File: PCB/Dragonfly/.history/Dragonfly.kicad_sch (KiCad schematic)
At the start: 201 parts, among them J1 Conn_01x04_Pin, J2 Micro_SD_Card, J3 Conn_01x02_Pin, J4 Conn_01x02_Pin, J5 Conn_01x02_Pin, J6 Conn_01x02_Pin, Q1 Q_NMOS_GDS, Q10 Q_NMOS_GDS, Q11 Q_NMOS_GDS, Q12 Q_NMOS_GDS, Q13 Q_NMOS_GDS, Q14 Q_NMOS_GDS, Q15 Q_NMOS_GDS, Q16 Q_NMOS_GDS, Q17 Q_NMOS_GDS, Q18 Q_NMOS_GDS, Q19 Q_NMOS_GDS, Q2 Q_NMOS_GDS, Q20 Q_NMOS_GDS, Q21 Q_NMOS_GDS, Q22 Q_NMOS_GDS, Q23 Q_NMOS_GDS, Q24 Q_NMOS_GDS, Q3 Q_NMOS_GDS, Q4 Q_NMOS_GDS, Q5 Q_NMOS_GDS, Q6 Q_NMOS_GDS, Q7 Q_NMOS_GDS, Q8 Q_NMOS_GDS, Q9 Q_NMOS_GDS, SW1 SW_SPST, SW2 SW_SPST, U1 STM32F405RGTx, U10 FD6288Q, U2 ICM-20602, U3 AT32F421G8U7, U4 FD6288Q, U5 AT32F421G8U7, U6 FD6288Q, U7 AT32F421G8U7, U8 FD6288Q, U9 AT32F421G8U7, X1 TSX-3225

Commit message: updates
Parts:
- removed D1: blue, symbol Device:D
- removed D2: red, symbol Device:D
- added C57, C60, C62: 10uf, symbol Device:C
- added C58: 0.01uf, symbol Device:C
- added C59: 220uf, symbol Device:C_US
- added C61, C63: 1uf, symbol Device:C
- added C64, C65: 100nf, symbol Device:C
- added D1: LED BLUE, symbol Device:LED
- added D15: 40V, 3A Schottky, Diode_SMD:D_SMC, symbol Diode:B340
- added D16: 40V, 3A Schottky, symbol Device:D_Schottky
- added D2: LED RED, symbol Device:LED
- added J7: Conn_01x02, symbol Connector_Generic:Conn_01x02
- added L2: 15uh, symbol Device:L_Ferrite
- added R87: 30.9k, symbol Device:R
- added R88: 10k, symbol Device:R
- added R89: 100k, symbol Device:R
- added U11: TPS5430DDA, Package_SO:TI_SO-PowerPAD-8_ThermalVias, symbol Regulator_Switching:TPS5430DDA
- added U12: AMS1117-3.3, Package_TO_SOT_SMD:SOT-223-3_TabPin2, symbol Regulator_Linear:AMS1117-3.3
- added U13: L78L08_SO8, Package_SO:SOIC-8_3.9x4.9mm_P1.27mm, symbol Regulator_Linear:L78L08_SO8
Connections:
- net +8V: now also C65.1, U13.1 (OUT)
- net GND: now also C57.2, C59.2, C64.2, C65.2, D1.2 (A), D15.2 (A), D2.2 (A), J7.2 (Pin_2), R88.2, U11.6 (GND), U11.9 (GNDPAD), U13.2 (GND), U13.3 (GND), U13.6 (GND), U13.7 (GND)
- net VDD33: now also C60.1, C61.1, U12.2 (VO)
- net VIN: now also C57.1, C64.1, D16.2 (A), R89.1, U11.7 (VIN), U13.8 (IN)
- net at R4.2: now also D1.1 (K)
- net at R5.2: now also D2.1 (K)
- new net: C60.2, C61.2, C62.2, C63.2
- new net: R89.2, U11.5 (EN)
- new net: R87.2, R88.1, U11.4 (VSENSE)
- new net: C58.1, U11.1 (BOOT)
- new net: C58.2, D15.1 (K), L2.1, U11.8 (PH)
- new net: D16.1 (K), J7.1 (Pin_1)
- new net VOUT: C59.1, C62.1, C63.1, L2.2, R87.1, U12.3 (VI)
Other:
- note added: "Battery connection"
- note added: "Power - Buck (5V) + LDO (3.3V)"
- moved on the sheet: C5, R1, R2, R3, R4, R5, SW1, SW2

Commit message: Update Dragonfly.kicad_sch
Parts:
- added C66, C67, C68, C69: 100nf, symbol Device:C
- added C70, C71: 47uf, symbol Device:C_Polarized
- added J10: USB_C_Receptacle_USB2.0_16P, symbol Connector:USB_C_Receptacle_USB2.0_16P
- added J8: VIN, symbol Connector:Conn_01x02_Socket
- added J9: VOUT, symbol Connector:Conn_01x02_Socket
- added R90, R91: 75 Ω, symbol Device:R
- added R92, R93: 22k, symbol Device:R
- added U14: AT7456E, SOP65P637X110-28N, symbol MAX7456EUI:MAX7456EUI+
- added Y1: 27MHZ, symbol Device:Crystal
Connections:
- net GND: now also C66.2, C67.2, C68.2, J10.A1 (GND), J10.A12 (GND), J10.B1 (GND), J10.B12 (GND), J10.SH (SHIELD), J8.2 (Pin_2), J9.2 (Pin_2), R90.2, U14.20 (AGND), U14.23 (PGND), U14.4 (DGND)
- net VIN: now also C69.1, U14.22 (VIN)
- net VOUT: now also C70.1, U14.26 (VOUT)
- net CS 1 renamed CS IMU
- net MISO renamed MISO IMU
- net MOSI renamed MOSI IMU
- net PB12 renamed CS SOD
- net CS SOD: now also U14.8 (~{CS})
- net PB13 renamed SCK SOD
- net SCK SOD: now also U14.10 (SCLK)
- net PB14 renamed MISO SOD
- net MISO SOD: now also U14.9 (SDIN)
- net PB15 renamed MOSI OSD
- net MOSI OSD: now also U14.11 (SDOUT)
- net SCK renamed SCK IMU
- new net: J9.1 (Pin_1), R91.1
- new net: C70.2, C71.2, R91.2
- new net: J10.A5 (CC1), R92.1
- new net: C69.2, J8.1 (Pin_1), R90.1
- new net: J10.B5 (CC2), R93.1
- new net +5V: J10.A4 (VBUS), J10.A9 (VBUS), J10.B4 (VBUS), J10.B9 (VBUS), R92.2, R93.2
- new net 5V: C66.1, C67.1, C68.1, U14.19 (~{RESET}), U14.21 (AVDD), U14.24 (PVDD), U14.3 (DVDD)
- new net D+: J10.A6 (D+), J10.B6 (D+)
- new net D-: J10.A7 (D-), J10.B7 (D-)
- new net SAG: C71.1, U14.25 (SAG)
- new net XTAL1: U14.5 (CLKIN), Y1.1
- new net XTAL2: U14.6 (XFB), Y1.2
- no-connect marks 44 -> 49
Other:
- note added: "OSD - AT7456E"
- note added: "USB-C 16pin"
- moved on the sheet: C20

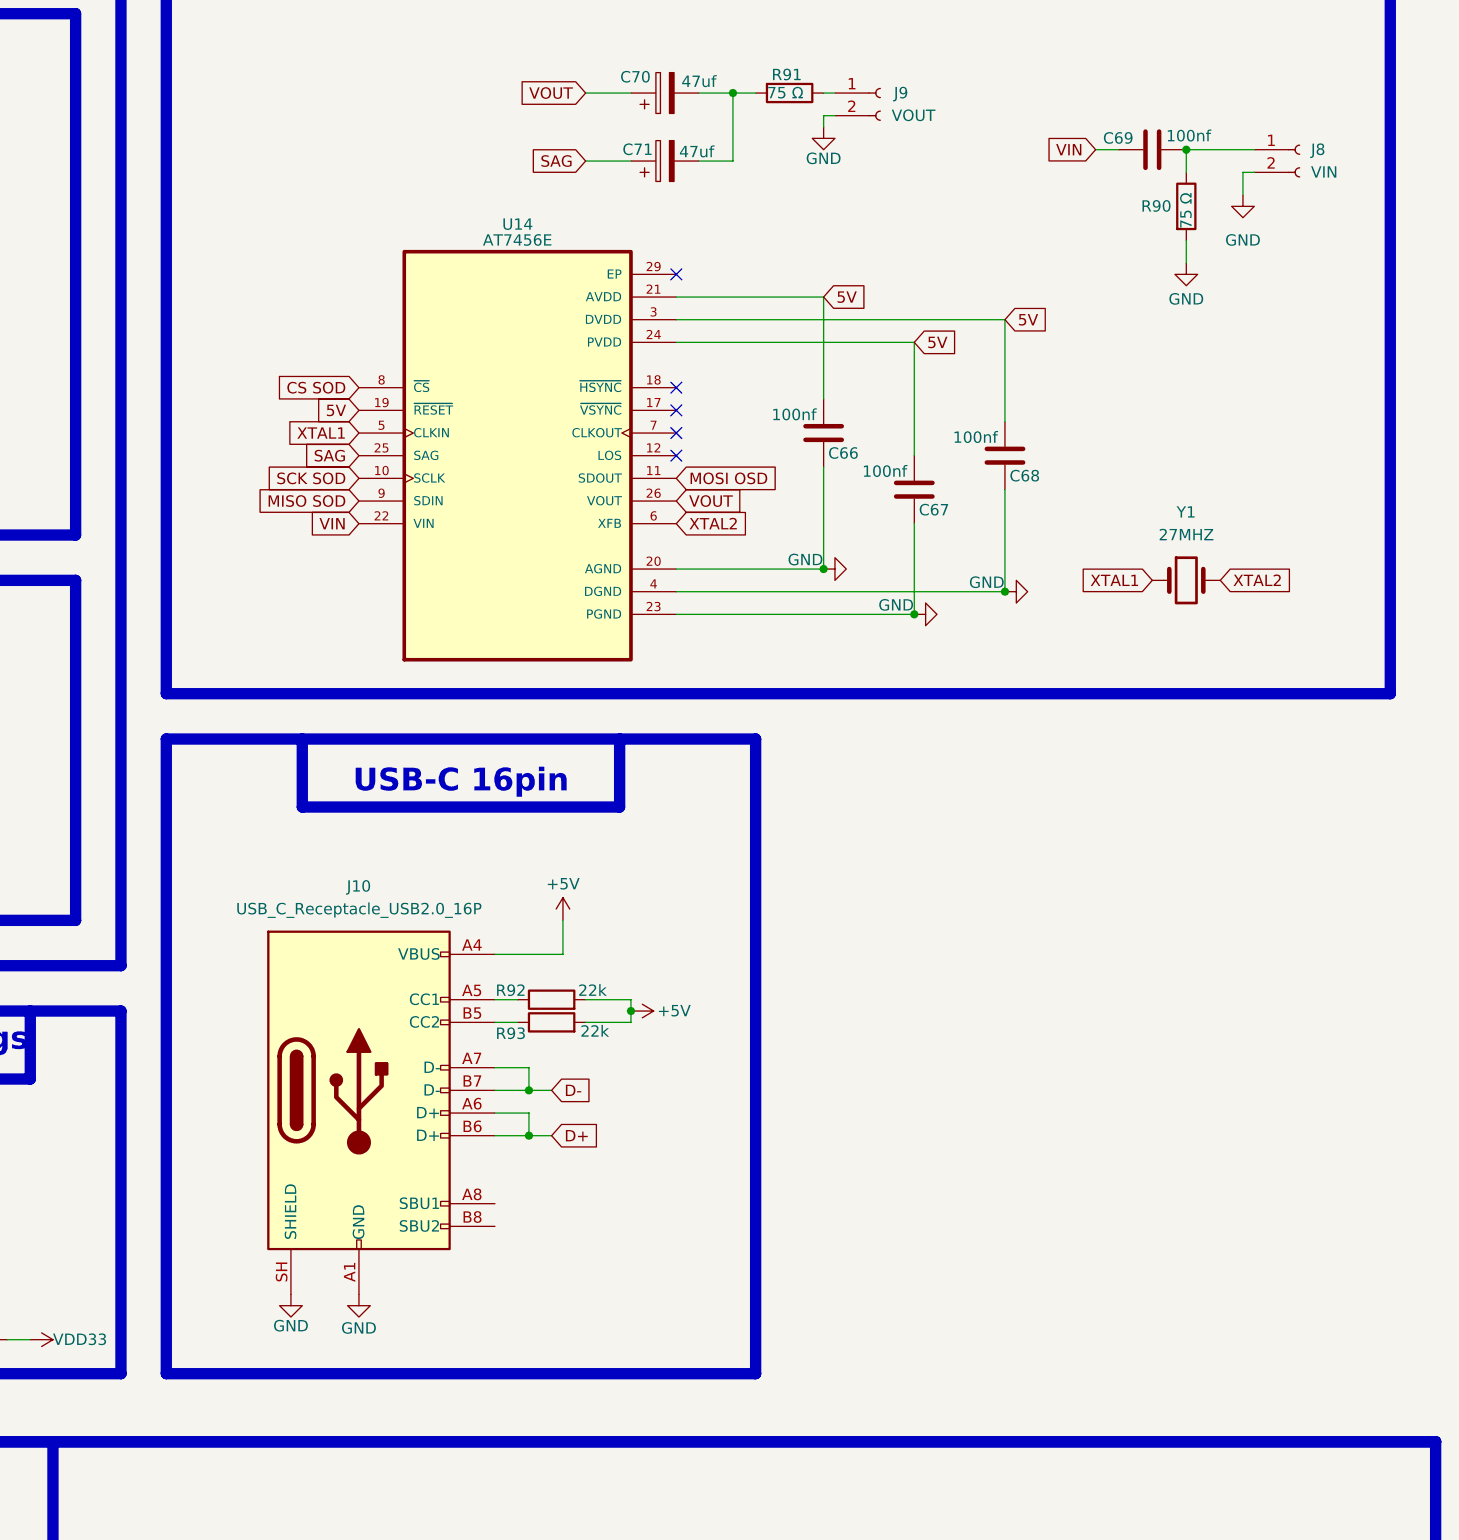
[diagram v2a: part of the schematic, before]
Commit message: Update Dragonfly.kicad_sch
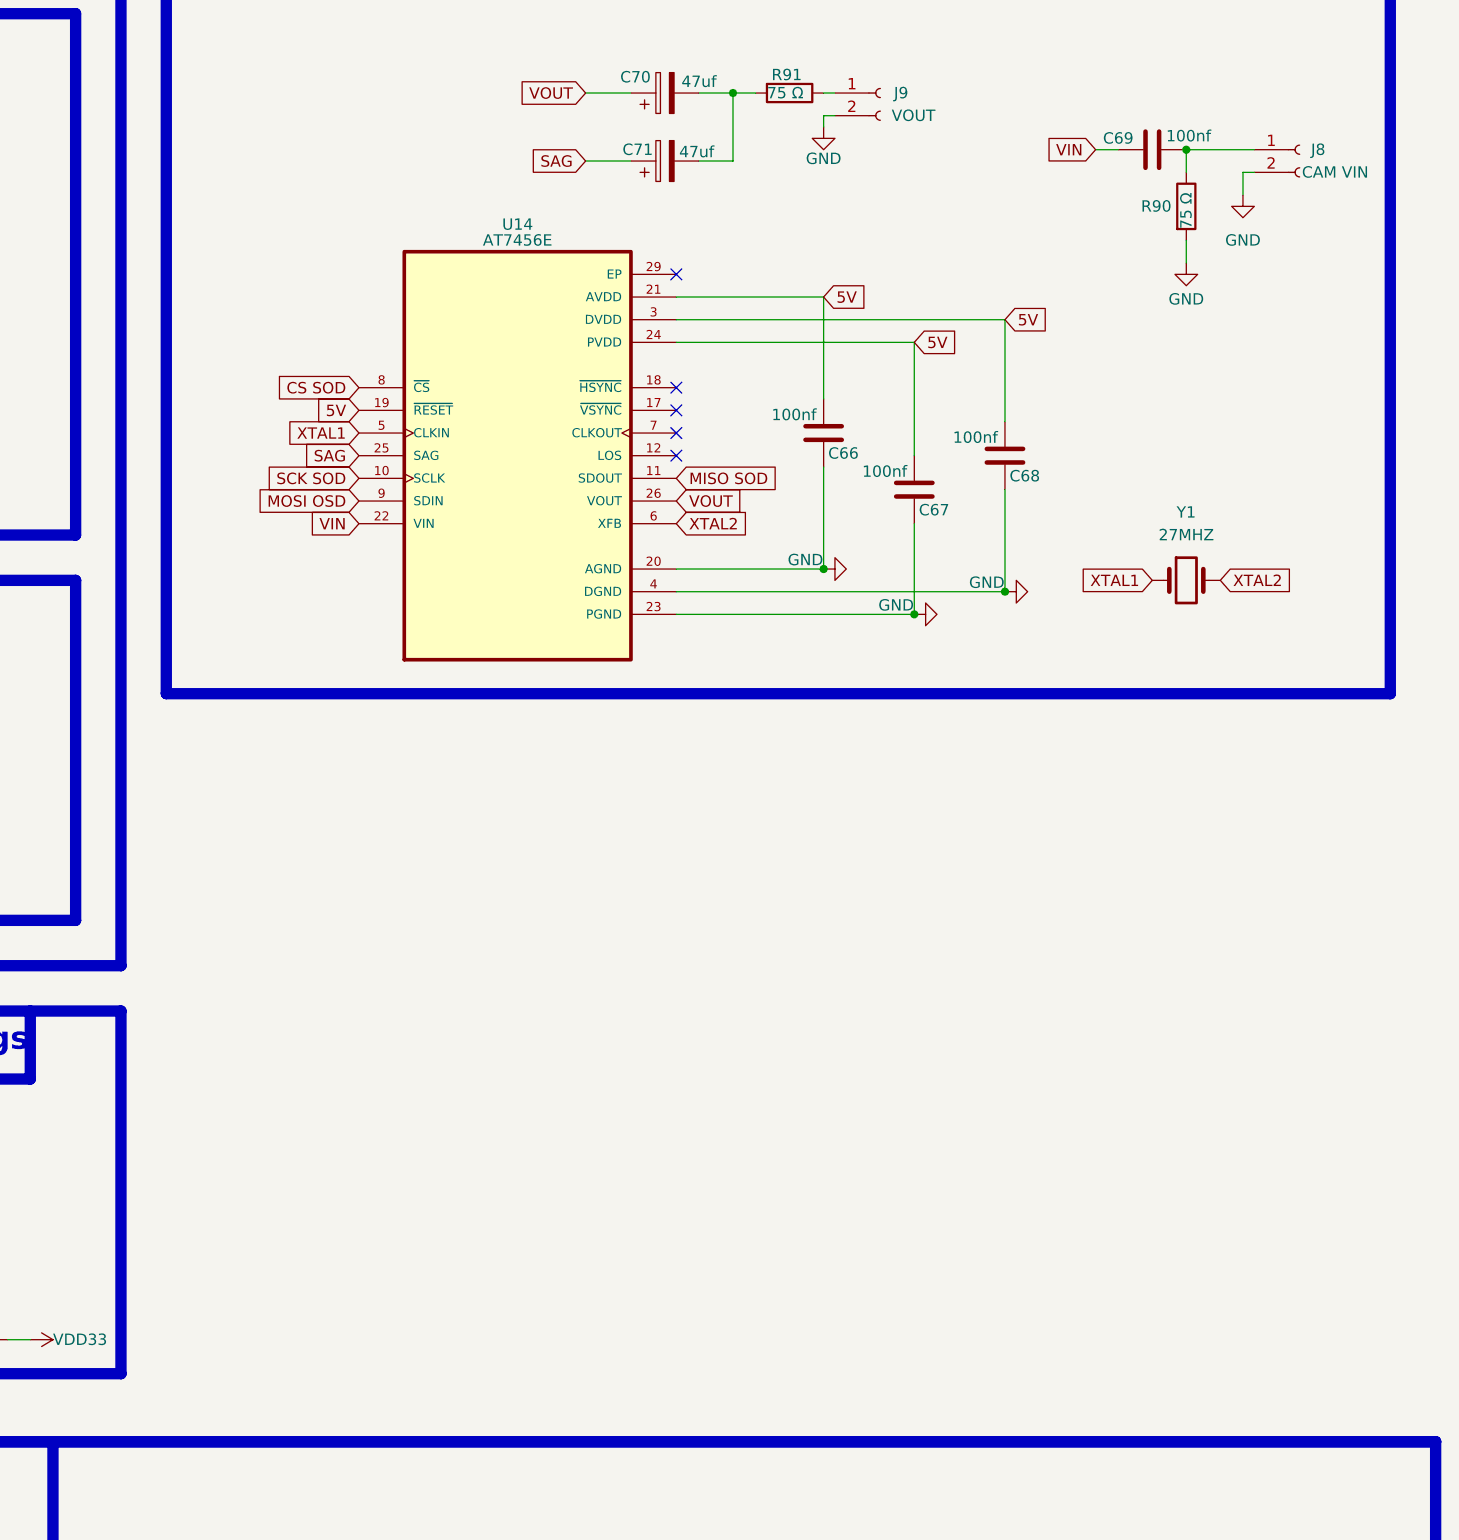
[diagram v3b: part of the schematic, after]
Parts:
- removed J10: USB_C_Receptacle_USB2.0_16P, symbol Connector:USB_C_Receptacle_USB2.0_16P
- removed R92, R93: 22k, symbol Device:R
- J8: value VIN -> CAM VIN
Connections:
- net MISO SOD: now also U14.11 (SDOUT); no longer U14.9 (SDIN)
- net MOSI OSD: now also U14.9 (SDIN); no longer U14.11 (SDOUT)
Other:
- note removed: "USB-C 16pin"

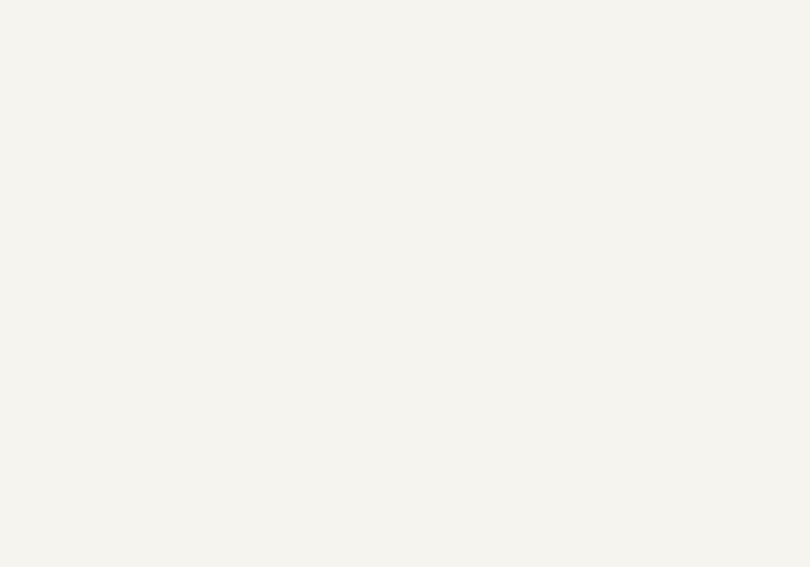
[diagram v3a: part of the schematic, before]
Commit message: Update Dragonfly.kicad_sch
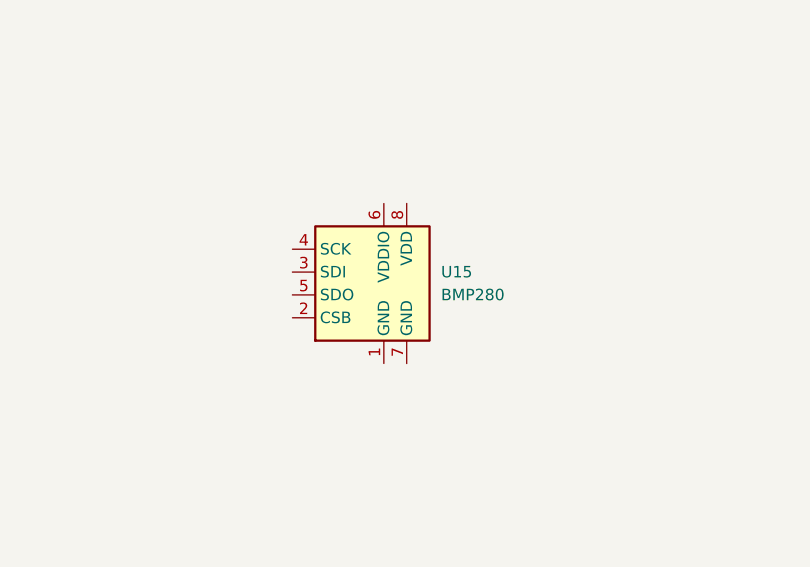
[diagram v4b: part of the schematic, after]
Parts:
- added U15: BMP280, Package_LGA:Bosch_LGA-8_2x2.5mm_P0.65mm_ClockwisePinNumbering, symbol Sensor_Pressure:BMP280
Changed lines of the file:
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@@
+	)
+	(symbol
+		(lib_id "Sensor_Pressure:BMP280")
+		(at 655.32 158.75 0)
+		(unit 1)
+		(body_style 1)
+		(exclude_from_sim no)
+		(in_bom yes)
+		(on_board yes)
+		(in_pos_files yes)
+		(dnp no)
+		(fields_autoplaced yes)
+		(property "Reference" "U15"
+			(at 661.67 156.2099 0)
+			(show_name no)
+			(do_not_autoplace no)
+			(effects
+				(font
+					(size 1.27 1.27)
+				)
+				(justify left)
+			)
+		)
+		(property "Value" "BMP280"
+			(at 661.67 158.7499 0)
+			(show_name no)
+			(do_not_autoplace no)
+			(effects
+				(font
+					(size 1.27 1.27)
+				)
+				(justify left)
+			)
+		)
+		(property "Footprint" "Package_LGA:Bosch_LGA-8_2x2.5mm_P0.65mm_ClockwisePinNumbering"
+			(at 655.32 176.53 0)
+			(hide yes)
+			(show_name no)
+			(do_not_autoplace no)
+			(effects
+				(font
+					(size 1.27 1.27)
+				)
+			)
+		)
+		(property "Datasheet" "https://ae-bst.resource.bosch.com/media/_tech/media/datasheets/BST-BMP280-DS001.pdf"
+			(at 655.32 158.75 0)
+			(hide yes)
+			(show_name no)
+			(do_not_autoplace no)
+			(effects
+				(font
+					(size 1.27 1.27)
+				)
+			)
+		)
+		(property "Description" "Absolute Barometric Pressure Sensor, LGA-8"
+			(at 655.32 158.75 0)
+			(hide yes)
+			(show_name no)
+			(do_not_autoplace no)
+			(effects
+				(font
+					(size 1.27 1.27)
+				)
+			)
+		)
+		(pin "6"
+		)
+		(pin "5"
+		)
+		(pin "8"
+		)
+		(pin "7"
+		)
+		(pin "1"
+		)
+		(pin "4"
+		)
+		(pin "2"
+		)
+		(pin "3"
+		)
+		(instances
+			(project "Dragonfly"
+				(path "/f0708a7e-abc5-4571-a850-719a309c37b6"
+					(reference "U15")
+					(unit 1)
+				)
+			)
+		)
 	)
 	(symbol

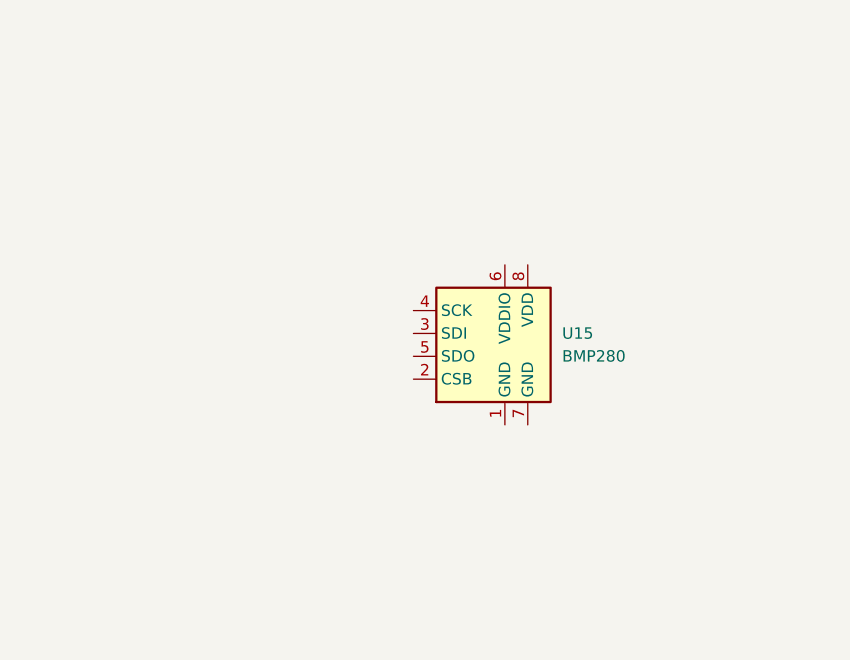
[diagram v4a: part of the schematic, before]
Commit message: Update Dragonfly.kicad_sch
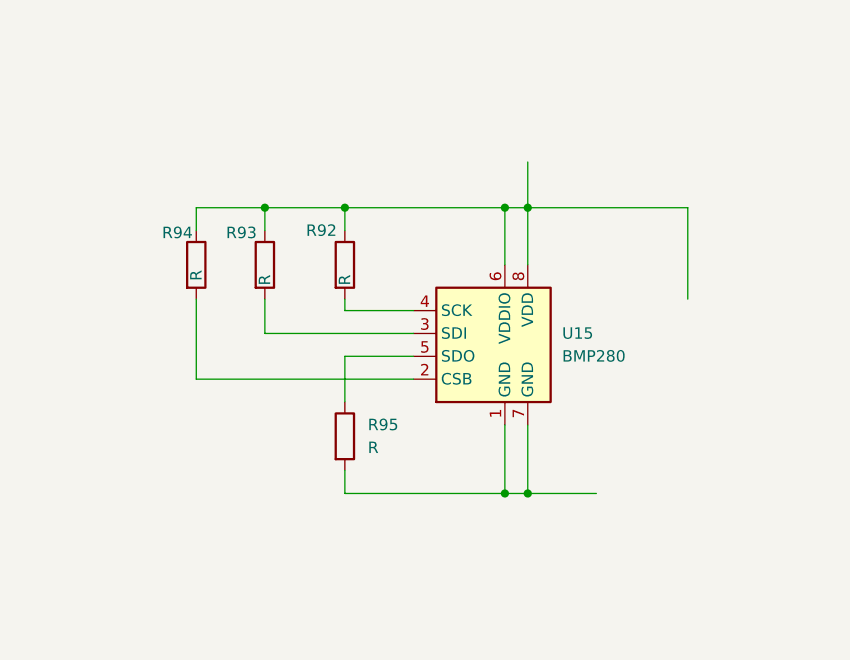
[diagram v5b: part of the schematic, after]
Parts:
- added R92, R93, R94, R95: R, symbol Device:R
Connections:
- net at U15.1 (GND): now also U15.7 (GND), R95.2
- net at U15.2 (CSB): now also R94.2
- net at U15.3 (SDI): now also R93.2
- net at U15.4 (SCK): now also R92.2
- net at U15.5 (SDO): now also R95.1
- net at U15.6 (VDDIO): now also U15.8 (VDD), R92.1, R93.1, R94.1

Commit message: Update Dragonfly.kicad_sch
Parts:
- added C72: 1uf, symbol Device:C
- added C73: 0.1uf, symbol Device:C
- R92, R93, R94, R95: value R -> 10k
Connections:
- net GND: now also R95.2, U15.1 (GND), U15.7 (GND), C72.2, C73.2
- net VDD33: now also R92.1, R93.1, R94.1, U15.6 (VDDIO), U15.8 (VDD), C72.1, C73.1
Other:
- note added: "BMP280 Barometer"

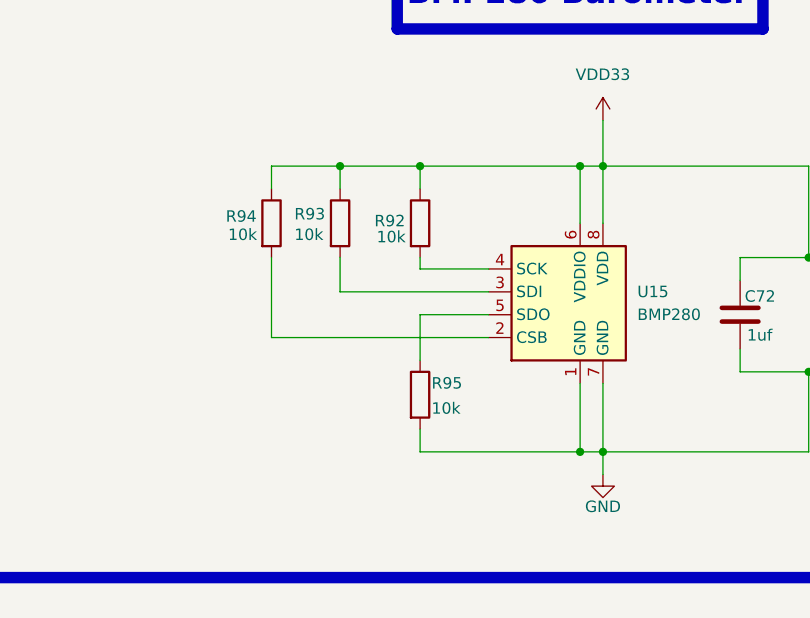
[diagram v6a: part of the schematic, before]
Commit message: Update Dragonfly.kicad_sch
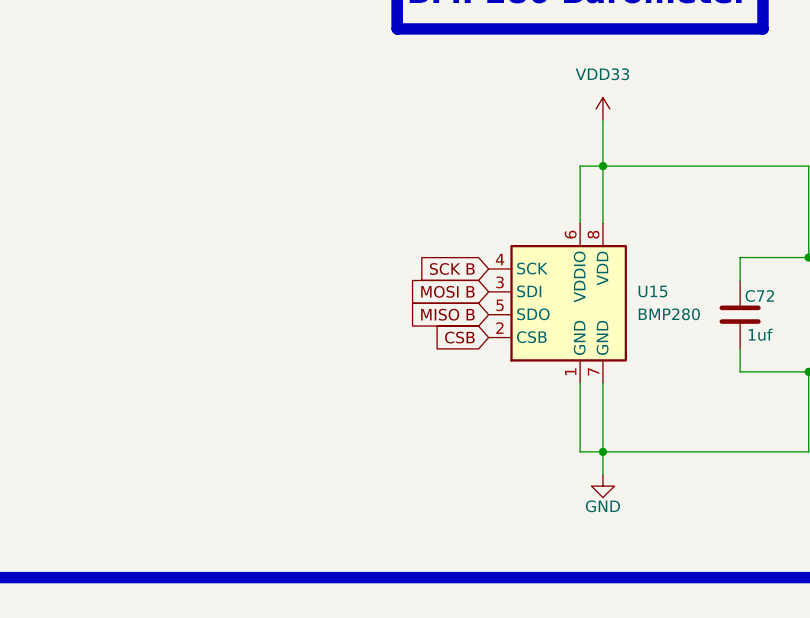
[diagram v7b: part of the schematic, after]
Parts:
- removed R92, R93, R94, R95: 10k, symbol Device:R
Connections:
- net CSB: now reaches U15.2 (CSB)
- net MOSI B: now reaches U15.3 (SDI)
- net SCK B: now reaches U15.4 (SCK)
- net MISO B: now reaches U15.5 (SDO)

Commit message: update
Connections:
- net PB5 is gone; now on net SCK B: U1.57 (PB5)
- net PB6 is gone; now on net MOSI B: U1.58 (PB6)
- net PB7 is gone; now on net MISO B: U1.59 (PB7)
- net PB8 is gone; now on net CSB: U1.61 (PB8)
- net VDD33A is gone; now on net VDD33: C13.1, C14.1, L1.2, U1.13 (VDDA)
- no-connect marks 49 -> 70
